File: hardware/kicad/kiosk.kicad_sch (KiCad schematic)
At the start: 17 parts, among them J10 Jack 5V rail 1, J11 Jack 5V rail 2, J12 Spare PCF8574, J13 PCF8574 0x20 - P0..P7, J3 LCD 4.0in ST7796S + GT911, J4 VL53L1X, J5 PCF8574 0x20 - I2C, J6 DS3231, J7 MAX98357A, J8 Speaker 4ohm 3W, J9 SG90 servo, U1 ESP32-S3-CAM N16R8

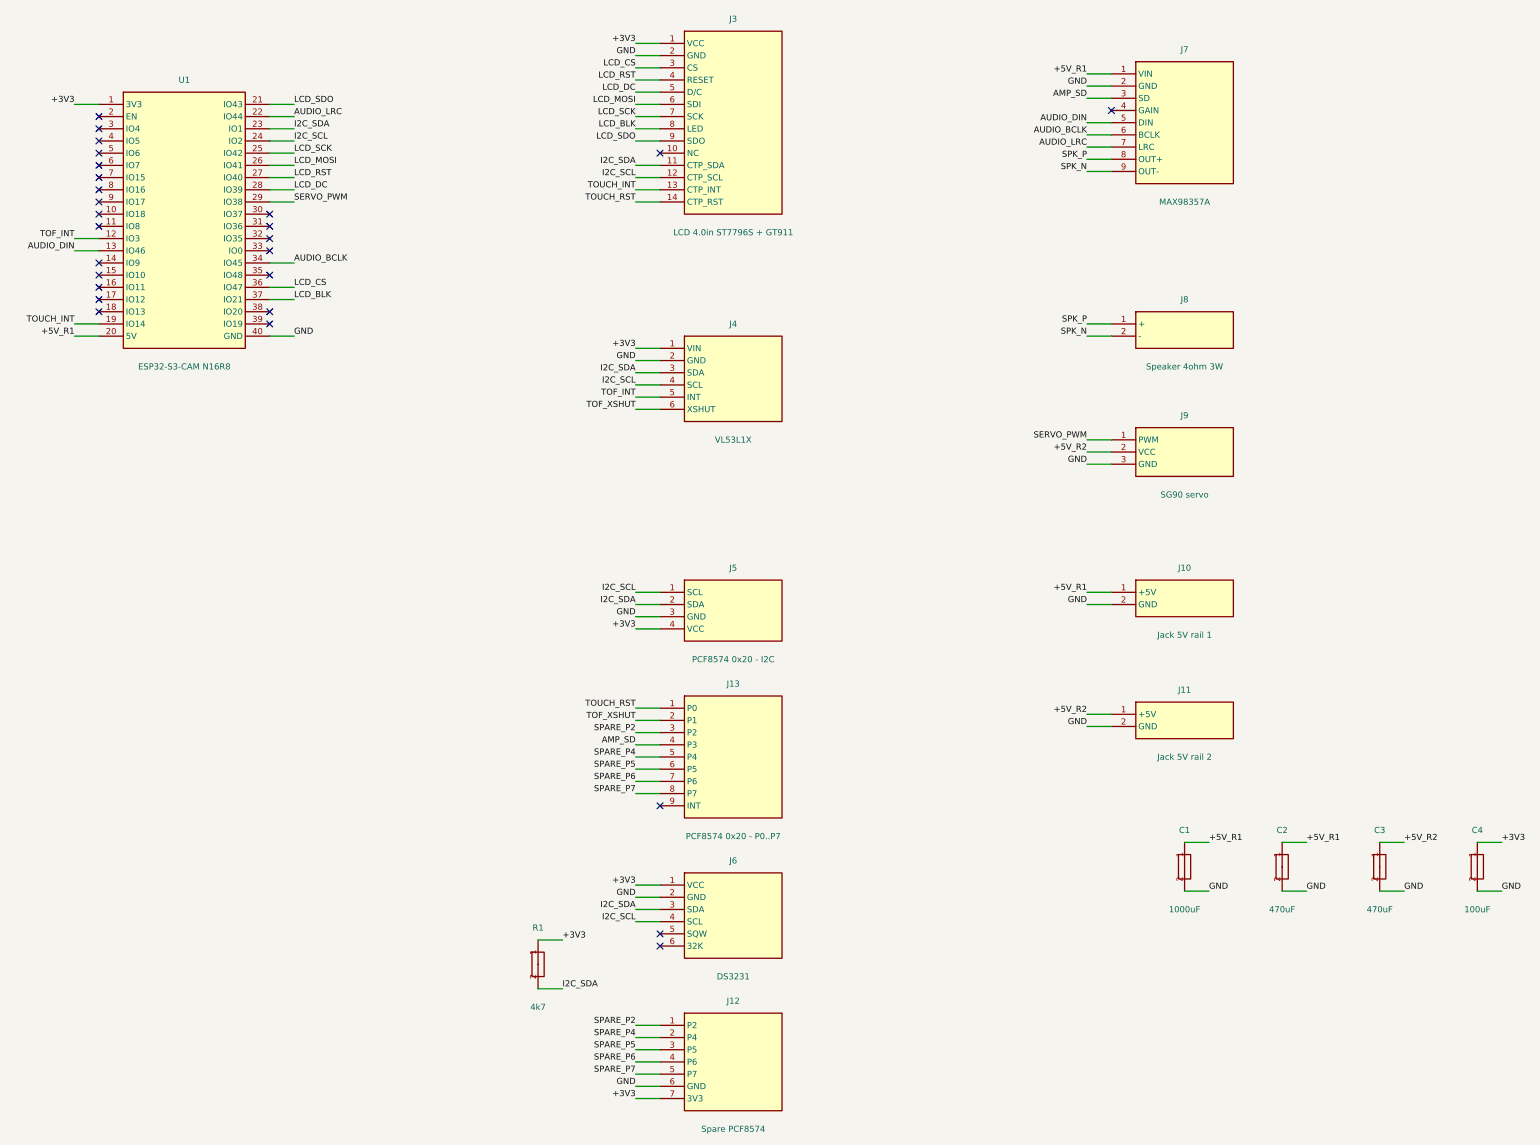
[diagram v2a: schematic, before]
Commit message: fix(hardware): take all three module pinouts off the parts, not off a guess
Photographs of the remaining three modules, and all three headers differ
from what the schematic said.

The ToF reads VIN GND SCL SDA GPIO1 XSHUT, so SDA and SCL were the wrong
way round. Its interrupt is silkscreened GPIO1, the sensor's own name for
it, which section 2.3D already warned has nothing to do with ESP GPIO1.

The RTC's six-pin row reads 32K SQW SCL SDA VCC GND, which is the reverse
of what was drawn, with the bus pair swapped inside it as well.

The amplifier is seven pins, not nine: LRC BCLK DIN GAIN SD GND Vin. The
two that were missing are the speaker output, and it is not on that header
at all - the module carries its own screw terminal on the opposite edge.
So the speaker wires land on the module and never reach the carrier, J8
goes, and with it the SPK_P and SPK_N nets.

Section 2.3 D, E and H now carry the header order as read off each part.
The tables there say where a pin goes; they never said in what order the
pins sit, which is the half a footprint needs.

Sixteen parts, twenty-seven nets, eighty-three connection points.
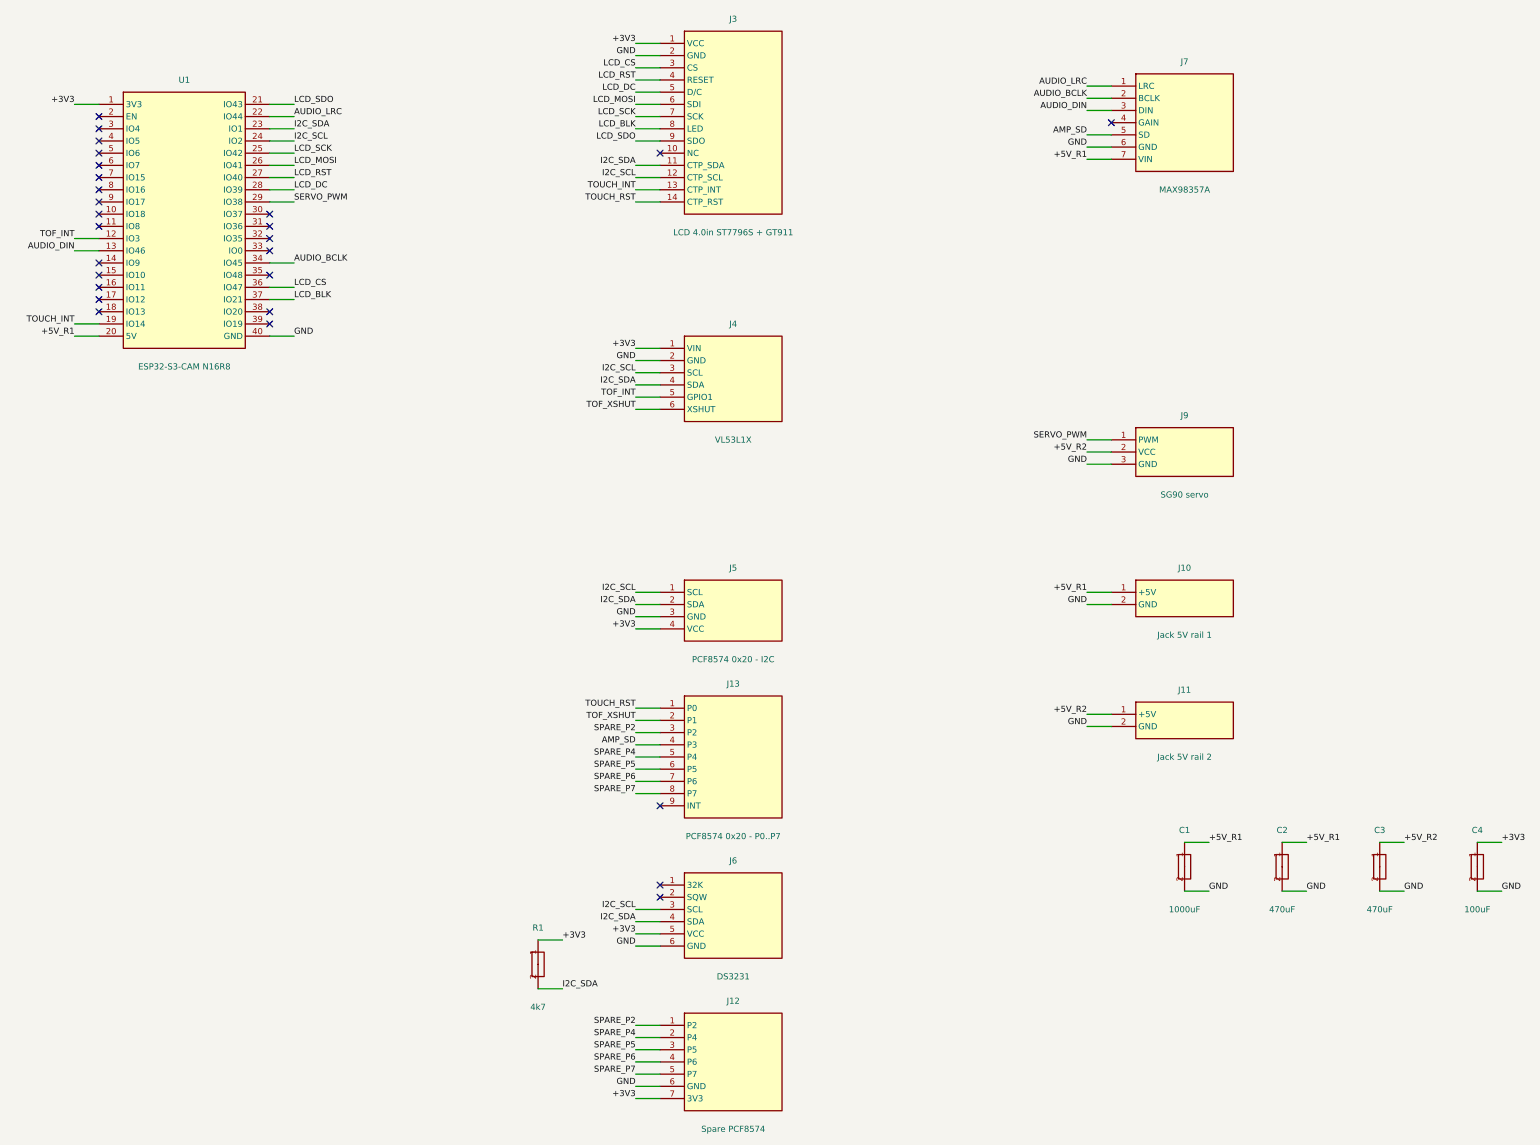
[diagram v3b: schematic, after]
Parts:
- removed J8: Speaker 4ohm 3W, TerminalBlock:TerminalBlock_MaiXu_MX126-5.0-02P_1x02_P5.00mm, symbol kiosk:J8
- J7: footprint Connector_PinSocket_2.54mm:PinSocket_1x09_P2.54mm_Vertical -> Connector_PinSocket_2.54mm:PinSocket_1x07_P2.54mm_Vertical
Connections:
- net +3V3: now also J6.5 (VCC); no longer J6.1 (VCC)
- net +5V_R1: now also J7.7 (VIN); no longer J7.1 (VIN)
- net AMP_SD: now also J7.5 (SD); no longer J7.3 (SD)
- net AUDIO_BCLK: now also J7.2 (BCLK); no longer J7.6 (BCLK)
- net AUDIO_DIN: now also J7.3 (DIN); no longer J7.5 (DIN)
- net AUDIO_LRC: now also J7.1 (LRC); no longer J7.7 (LRC)
- net GND: now also J6.6 (GND), J7.6 (GND); no longer J6.2 (GND), J7.2 (GND)
- net I2C_SCL: now also J4.3 (SCL), J6.3 (SCL); no longer J4.4 (SCL), J6.4 (SCL)
- net I2C_SDA: now also J4.4 (SDA), J6.4 (SDA); no longer J4.3 (SDA), J6.3 (SDA)
- removed net SPK_N: J7.9 (OUT-)
- removed net SPK_P: J7.8 (OUT+)
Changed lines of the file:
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@@
   (wire (pts (xy 175.26 92.71000000000001) (xy 170.17999999999998 92.71000000000001))
     (stroke (width 0) (type default)))
-  (label "I2C_SDA" (at 170.17999999999998 92.71000000000001 180)
+  (label "I2C_SCL" (at 170.17999999999998 92.71000000000001 180)
     (effects (font (size 1.27 1.27)) (justify right bottom))
 )
   (wire (pts (xy 175.26 95.25000000000001) (xy 170.17999999999998 95.25000000000001))
     (stroke (width 0) (type default)))
-  (label "I2C_SCL" (at 170.17999999999998 95.25000000000001 180)
+  (label "I2C_SDA" (at 170.17999999999998 95.25000000000001 180)
     (effects (font (size 1.27 1.27)) (justify right bottom))
 )
@@
     )
   )
-  (wire (pts (xy 175.26 199.39000000000001) (xy 170.17999999999998 199.39000000000001))
-    (stroke (width 0) (type default)))
-  (label "+3V3" (at 170.17999999999998 199.39000000000001 180)
-    (effects (font (size 1.27 1.27)) (justify right bottom))
-)
-  (wire (pts (xy 175.26 201.93) (xy 170.17999999999998 201.93))
-    (stroke (width 0) (type default)))
-  (label "GND" (at 170.17999999999998 201.93 180)
-    (effects (font (size 1.27 1.27)) (justify right bottom))
-)
+  (no_connect (at 175.26 199.39000000000001))
+  (no_connect (at 175.26 201.93))
   (wire (pts (xy 175.26 204.47000000000003) (xy 170.17999999999998 204.47000000000003))
     (stroke (width 0) (type default)))
-  (label "I2C_SDA" (at 170.17999999999998 204.47000000000003 180)
+  (label "I2C_SCL" (at 170.17999999999998 204.47000000000003 180)
     (effects (font (size 1.27 1.27)) (justify right bottom))
 )
   (wire (pts (xy 175.26 207.01000000000002) (xy 170.17999999999998 207.01000000000002))
     (stroke (width 0) (type default)))
-  (label "I2C_SCL" (at 170.17999999999998 207.01000000000002 180)
-    (effects (font (size 1.27 1.27)) (justify right bottom))
-)
-  (no_connect (at 175.26 209.55))
-  (no_connect (at 175.26 212.09))
+  (label "I2C_SDA" (at 170.17999999999998 207.01000000000002 180)
+    (effects (font (size 1.27 1.27)) (justify right bottom))
+)
+  (wire (pts (xy 175.26 209.55) (xy 170.17999999999998 209.55))
+    (stroke (width 0) (type default)))
+  (label "+3V3" (at 170.17999999999998 209.55 180)
+    (effects (font (size 1.27 1.27)) (justify right bottom))
+)
+  (wire (pts (xy 175.26 212.09) (xy 170.17999999999998 212.09))
+    (stroke (width 0) (type default)))
+  (label "GND" (at 170.17999999999998 212.09 180)
+    (effects (font (size 1.27 1.27)) (justify right bottom))
+)
   (symbol (lib_id "kiosk:J7") (at 284.48 40.64 0) (unit 1)
     (exclude_from_sim no) (in_bom yes) (on_board yes) (dnp no)
-    (property "Reference" "J7" (at 284.48 25.4 0) (effects (font (size 1.27 1.27))))
-    (property "Value" "MAX98357A" (at 284.48 57.15 0) (effects (font (size 1.27 1.27))))
-    (property "Footprint" "Connector_PinSocket_2.54mm:PinSocket_1x09_P2.54mm_Vertical" (at 284.48 40.64 0)
+    (property "Reference" "J7" (at 284.48 27.940000000000005 0) (effects (font (size 1.27 1.27))))
+    (property "Value" "MAX98357A" (at 284.48 54.61 0) (effects (font (size 1.27 1.27))))
+    (property "Footprint" "Connector_PinSocket_2.54mm:PinSocket_1x07_P2.54mm_Vertical" (at 284.48 40.64 0)
       (effects (font (size 1.27 1.27)) hide))
     (property "Datasheet" "" (at 284.48 40.64 0) (effects (font (size 1.27 1.27)) hide))
@@
     (pin "6")
     (pin "7")
-    (pin "8")
-    (pin "9")
     (instances
       (project "kiosk"
@@
     )
   )
-  (wire (pts (xy 269.24 30.48) (xy 264.16 30.48))
-    (stroke (width 0) (type default)))
-  (label "+5V_R1" (at 264.16 30.48 180)
-    (effects (font (size 1.27 1.27)) (justify right bottom))
-)
   (wire (pts (xy 269.24 33.02) (xy 264.16 33.02))
     (stroke (width 0) (type default)))
-  (label "GND" (at 264.16 33.02 180)
+  (label "AUDIO_LRC" (at 264.16 33.02 180)
     (effects (font (size 1.27 1.27)) (justify right bottom))
 )
   (wire (pts (xy 269.24 35.56) (xy 264.16 35.56))
     (stroke (width 0) (type default)))
-  (label "AMP_SD" (at 264.16 35.56 180)
-    (effects (font (size 1.27 1.27)) (justify right bottom))
-)
-  (no_connect (at 269.24 38.1))
-  (wire (pts (xy 269.24 40.64) (xy 264.16 40.64))
-    (stroke (width 0) (type default)))
-  (label "AUDIO_DIN" (at 264.16 40.64 180)
-    (effects (font (size 1.27 1.27)) (justify right bottom))
-)
-  (wire (pts (xy 269.24 43.18) (xy 264.16 43.18))
-    (stroke (width 0) (type default)))
-  (label "AUDIO_BCLK" (at 264.16 43.18 180)
+  (label "AUDIO_BCLK" (at 264.16 35.56 180)
+    (effects (font (size 1.27 1.27)) (justify right bottom))
+)
+  (wire (pts (xy 269.24 38.1) (xy 264.16 38.1))
+    (stroke (width 0) (type default)))
+  (label "AUDIO_DIN" (at 264.16 38.1 180)
+    (effects (font (size 1.27 1.27)) (justify right bottom))
+)
+  (no_connect (at 269.24 40.64))
+  (wire (pts (xy 269.24 43.18000000000001) (xy 264.16 43.18000000000001))
+    (stroke (width 0) (type default)))
+  (label "AMP_SD" (at 264.16 43.18000000000001 180)
     (effects (font (size 1.27 1.27)) (justify right bottom))
 )
   (wire (pts (xy 269.24 45.72) (xy 264.16 45.72))
     (stroke (width 0) (type default)))
-  (label "AUDIO_LRC" (at 264.16 45.72 180)
+  (label "GND" (at 264.16 45.72 180)
     (effects (font (size 1.27 1.27)) (justify right bottom))
 )
   (wire (pts (xy 269.24 48.260000000000005) (xy 264.16 48.260000000000005))
     (stroke (width 0) (type default)))
-  (label "SPK_P" (at 264.16 48.260000000000005 180)
-    (effects (font (size 1.27 1.27)) (justify right bottom))
-)
-  (wire (pts (xy 269.24 50.8) (xy 264.16 50.8))
-    (stroke (width 0) (type default)))
-  (label "SPK_N" (at 264.16 50.8 180)
-    (effects (font (size 1.27 1.27)) (justify right bottom))
-)
-  (symbol (lib_id "kiosk:J8") (at 284.48 83.82 0) (unit 1)
-    (exclude_from_sim no) (in_bom yes) (on_board yes) (dnp no)
-    (property "Reference" "J8" (at 284.48 77.47 0) (effects (font (size 1.27 1.27))))
-    (property "Value" "Speaker 4ohm 3W" (at 284.48 91.43999999999998 0) (effects (font (size 1.27 1.27))))
-    (property "Footprint" "TerminalBlock:TerminalBlock_MaiXu_MX126-5.0-02P_1x02_P5.00mm" (at 284.48 83.82 0)
-      (effects (font (size 1.27 1.27)) hide))
-    (property "Datasheet" "" (at 284.48 83.82 0) (effects (font (size 1.27 1.27)) hide))
-    (pin "1")
-    (pin "2")
-    (instances
-      (project "kiosk"
-        (path "/b0a1c2d3-0000-4000-8000-000000000001" (reference "J8") (unit 1))
-      )
-    )
-  )
-  (wire (pts (xy 269.24 82.55) (xy 264.16 82.55))
-    (stroke (width 0) (type default)))
-  (label "SPK_P" (at 264.16 82.55 180)
-    (effects (font (size 1.27 1.27)) (justify right bottom))
-)
-  (wire (pts (xy 269.24 85.09) (xy 264.16 85.09))
-    (stroke (width 0) (type default)))
-  (label "SPK_N" (at 264.16 85.09 180)
-    (effects (font (size 1.27 1.27)) (justify right bottom))
-)
+  (label "+5V_R1" (at 264.16 48.260000000000005 180)
+    (effects (font (size 1.27 1.27)) (justify right bottom))
+)

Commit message: fix(hardware): the servo header was drawn back to front
J9 read PWM, VCC, GND. An SG90 plug reads brown ground, red supply,
orange signal - ground and signal at the two ends with the supply between
them. Only the middle pin agreed, so plugging the servo in the one way it
fits would have put its ground onto the pin GPIO38 drives and its signal
input onto ground: no movement, and an output driving into a ground
return.

Section 2.3F now carries the plug order beside the table, which said
correctly where each wire goes and never said in what order they arrive.
That is the fourth connector this session whose order came from reading a
table rather than the part.

The servo itself bolts to the enclosure by its own two tabs, next to the
barrier it swings; only its lead reaches the board.
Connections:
- net GND: now also J9.1 (GND); no longer J9.3 (GND)
- net SERVO_PWM: now also J9.3 (PWM); no longer J9.1 (PWM)
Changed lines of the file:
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@@
   (wire (pts (xy 269.24 106.67999999999999) (xy 264.16 106.67999999999999))
     (stroke (width 0) (type default)))
-  (label "SERVO_PWM" (at 264.16 106.67999999999999 180)
+  (label "GND" (at 264.16 106.67999999999999 180)
     (effects (font (size 1.27 1.27)) (justify right bottom))
 )
@@
   (wire (pts (xy 269.24 111.75999999999999) (xy 264.16 111.75999999999999))
     (stroke (width 0) (type default)))
-  (label "GND" (at 264.16 111.75999999999999 180)
+  (label "SERVO_PWM" (at 264.16 111.75999999999999 180)
     (effects (font (size 1.27 1.27)) (justify right bottom))
 )

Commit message: docs(hardware): name the three expander connectors for what each one is
J12 and J13 both showed a row of P pins and read as duplicates. They are
not. J13 is the socket the module drops into; J12 brings the spare port
pins back out, because once the module is seated it covers J13 and those
pins can no longer be reached. Section 2.4 leaves no general-purpose GPIO
free, so that row is the only way the board grows later.

The labels now say which is the socket and which is the breakout.
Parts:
- J12: value Spare PCF8574 -> Mo rong: P2,P4..P7 dua ra
- J13: value PCF8574 0x20 - P0..P7 -> PCF8574 0x20 - de cam hang P
- J5: value PCF8574 0x20 - I2C -> PCF8574 0x20 - de cam hang I2C
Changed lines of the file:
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@@
     (exclude_from_sim no) (in_bom yes) (on_board yes) (dnp no)
     (property "Reference" "J5" (at 190.5 133.35 0) (effects (font (size 1.27 1.27))))
-    (property "Value" "PCF8574 0x20 - I2C" (at 190.5 152.4 0) (effects (font (size 1.27 1.27))))
+    (property "Value" "PCF8574 0x20 - de cam hang I2C" (at 190.5 152.4 0) (effects (font (size 1.27 1.27))))
     (property "Footprint" "Connector_PinSocket_2.54mm:PinSocket_1x04_P2.54mm_Vertical" (at 190.5 142.24 0)
       (effects (font (size 1.27 1.27)) hide))
@@
     (exclude_from_sim no) (in_bom yes) (on_board yes) (dnp no)
     (property "Reference" "J13" (at 190.5 157.48 0) (effects (font (size 1.27 1.27))))
-    (property "Value" "PCF8574 0x20 - P0..P7" (at 190.5 189.23 0) (effects (font (size 1.27 1.27))))
+    (property "Value" "PCF8574 0x20 - de cam hang P" (at 190.5 189.23 0) (effects (font (size 1.27 1.27))))
     (property "Footprint" "Connector_PinSocket_2.54mm:PinSocket_1x09_P2.54mm_Vertical" (at 190.5 172.72 0)
       (effects (font (size 1.27 1.27)) hide))
@@
     (exclude_from_sim no) (in_bom yes) (on_board yes) (dnp no)
     (property "Reference" "J12" (at 190.5 223.51999999999998 0) (effects (font (size 1.27 1.27))))
-    (property "Value" "Spare PCF8574" (at 190.5 250.19 0) (effects (font (size 1.27 1.27))))
+    (property "Value" "Mo rong: P2,P4..P7 dua ra" (at 190.5 250.19 0) (effects (font (size 1.27 1.27))))
     (property "Footprint" "Connector_PinHeader_2.54mm:PinHeader_1x07_P2.54mm_Vertical" (at 190.5 236.22 0)
       (effects (font (size 1.27 1.27)) hide))

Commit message: feat(hardware): wire the expander's port pins instead of socketing them
The expander is the one module whose two rows point ninety degrees apart:
four bus pins lying in the plane of its board, nine port pins standing up
out of it. No way round is both of them down, so it cannot seat on two
sockets however it is turned.

The bus row seats on J5 as before. The port signals become wire: plugged
onto the module at one end, stripped and soldered into J13 at the other.
That is the better joint anyway - P0 resets the touch controller, and
section 2.3C records that a loose contact there reads exactly like a
logic fault and costs a day.

J13 therefore moves out from under the module, into the gap between it
and the RTC, where wires can reach it.

Recorded with it: the module now rests on four pins at one end with 48 mm
cantilevered off the other, and this board carries a servo. The far end
needs a standoff.
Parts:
- J13: value PCF8574 0x20 - de cam hang P -> PCF8574: han day tu hang P sang day; footprint Connector_PinSocket_2.54mm:PinSocket_1x09_P2.54mm_Vertical -> Connector_PinHeader_2.54mm:PinHeader_1x09_P2.54mm_Vertical
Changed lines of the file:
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@@
     (exclude_from_sim no) (in_bom yes) (on_board yes) (dnp no)
     (property "Reference" "J13" (at 190.5 157.48 0) (effects (font (size 1.27 1.27))))
-    (property "Value" "PCF8574 0x20 - de cam hang P" (at 190.5 189.23 0) (effects (font (size 1.27 1.27))))
-    (property "Footprint" "Connector_PinSocket_2.54mm:PinSocket_1x09_P2.54mm_Vertical" (at 190.5 172.72 0)
+    (property "Value" "PCF8574: han day tu hang P sang day" (at 190.5 189.23 0) (effects (font (size 1.27 1.27))))
+    (property "Footprint" "Connector_PinHeader_2.54mm:PinHeader_1x09_P2.54mm_Vertical" (at 190.5 172.72 0)
       (effects (font (size 1.27 1.27)) hide))
     (property "Datasheet" "" (at 190.5 172.72 0) (effects (font (size 1.27 1.27)) hide))
